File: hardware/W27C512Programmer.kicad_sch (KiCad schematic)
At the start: 124 parts, among them J1 CTRL, J2 MSB, J3 LSB, J4 Ext_UART, J5 OLED, J6 VP, J7 SAO, J8 Conn_01x02, Q1 MMBT3904, Q10 MMBT3906, Q11 MMBT3904, Q12 MMBT3906, Q2 MMBT3906, Q3 MMBT3904, Q4 MMBT3904, Q5 MMBT3904, Q6 MMBT3906, Q7 MMBT3906, Q8 MMBT3906, Q9 MMBT3904, SW1 RST, SW2 USR, U1 MIC2288, U2 74HC573, U3 74HC573, U4 74HC573, U5 28/32 pin ROM

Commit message: Rev2
Untested!
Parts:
- A1, C11, J1, J2, J3, J4, J5, J6, J7, J8, JP4, JP5, U5: now not fitted
- C10: footprint Capacitor_SMD:CP_Elec_6.3x5.4 -> Capacitor_SMD:CP_Elec_6.3x7.7; LCSC C131120 -> C22388053
- C12, C2, C3, C4, C5, C6, C7, C8: footprint Capacitor_SMD:C_0603_1608Metric -> Capacitor_SMD:C_0402_1005Metric; LCSC (none) -> C1525
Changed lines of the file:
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@@
 	(wire
 		(pts
-			(xy 270.51 48.26) (xy 282.956 48.26)
+			(xy 270.51 48.26) (xy 283.21 48.26)
 		)
 		(stroke
@@
 	(wire
 		(pts
-			(xy 274.574 82.296) (xy 282.956 82.296)
+			(xy 274.574 82.296) (xy 283.21 82.296)
 		)
 		(stroke
@@
 	(wire
 		(pts
-			(xy 282.956 82.296) (xy 282.956 48.26)
+			(xy 283.21 82.296) (xy 283.21 48.26)
 		)
 		(stroke
@@
 		(in_bom yes)
 		(on_board yes)
-		(dnp no)
+		(dnp yes)
 		(property "Reference" "J6"
 			(at 194.945 119.38 0)
@@
 		(in_bom yes)
 		(on_board yes)
-		(dnp no)
+		(dnp yes)
 		(fields_autoplaced yes)
 		(property "Reference" "J7"
@@
 			)
 		)
-		(property "Footprint" "Capacitor_SMD:C_0603_1608Metric"
+		(property "Footprint" "Capacitor_SMD:C_0402_1005Metric"
 			(at 21.59 102.87 0)
 			(effects
@@
 			)
 		)
+		(property "LCSC" "C1525"
+			(at 21.59 102.87 0)
+			(effects
+				(font
+					(size 1.27 1.27)
+				)
+				(hide yes)
+			)
+		)
 		(pin "1"
 		)
@@
 		(in_bom yes)
 		(on_board yes)
-		(dnp no)
+		(dnp yes)
 		(property "Reference" "J2"
 			(at 22.225 45.085 0)
@@
 			)
 		)
-		(property "Footprint" "Capacitor_SMD:C_0603_1608Metric"
+		(property "Footprint" "Capacitor_SMD:C_0402_1005Metric"
 			(at 69.85 102.87 0)
 			(effects
@@
 			)
 		)
+		(property "LCSC" "C1525"
+			(at 69.85 102.87 0)
+			(effects
+				(font
+					(size 1.27 1.27)
+				)
+				(hide yes)
+			)
+		)
 		(pin "1"
 		)
@@
 		(in_bom yes)
 		(on_board yes)
-		(dnp no)
+		(dnp yes)
 		(property "Reference" "J3"
 			(at 30.48 20.32 0)
@@
 		(in_bom yes)
 		(on_board yes)
-		(dnp no)
+		(dnp yes)
 		(fields_autoplaced yes)
 		(property "Reference" "J4"
@@
 			)
 		)
-		(property "Footprint" "Capacitor_SMD:C_0603_1608Metric"
+		(property "Footprint" "Capacitor_SMD:C_0402_1005Metric"
 			(at 49.53 102.87 0)
 			(effects
@@
 			)
 		)
+		(property "LCSC" "C1525"
+			(at 49.53 102.87 0)
+			(effects
+				(font
+					(size 1.27 1.27)
+				)
+				(hide yes)
+			)
+		)
 		(pin "1"
 		)
@@
 			)
 		)
-		(property "Footprint" "Capacitor_SMD:C_0603_1608Metric"
+		(property "Footprint" "Capacitor_SMD:C_0402_1005Metric"
 			(at 43.18 102.87 0)
 			(effects
@@
 			)
 		)
+		(property "LCSC" "C1525"
+			(at 43.18 102.87 0)
+			(effects
+				(font
+					(size 1.27 1.27)
+				)
+				(hide yes)
+			)
+		)
 		(pin "1"
 		)
@@
 		(in_bom yes)
 		(on_board yes)
-		(dnp no)
+		(dnp yes)
 		(fields_autoplaced yes)
 		(property "Reference" "J8"
@@
 		(in_bom yes)
 		(on_board yes)
-		(dnp no)
+		(dnp yes)
 		(fields_autoplaced yes)
 		(property "Reference" "J1"
@@
 			)
 		)
-		(property "Footprint" "Capacitor_SMD:C_0603_1608Metric"
+		(property "Footprint" "Capacitor_SMD:C_0402_1005Metric"
 			(at 27.94 102.87 0)
 			(effects
@@
 			)
 		)
+		(property "LCSC" "C1525"
+			(at 27.94 102.87 0)
+			(effects
+				(font
+					(size 1.27 1.27)
+				)
+				(hide yes)
+			)
+		)
 		(pin "1"
 		)
@@
 		(in_bom yes)
 		(on_board yes)
-		(dnp no)
+		(dnp yes)
 		(property "Reference" "JP4"
 			(at 179.07 64.77 0)
@@
 			)
 		)
-		(property "Footprint" "Capacitor_SMD:C_0603_1608Metric"
+		(property "Footprint" "Capacitor_SMD:C_0402_1005Metric"
 			(at 55.88 102.87 0)
 			(effects
@@
 			)
 		)
+		(property "LCSC" "C1525"
+			(at 55.88 102.87 0)
+			(effects
+				(font
+					(size 1.27 1.27)
+				)
+				(hide yes)
+			)
+		)
 		(pin "1"
 		)
@@
 		(in_bom yes)
 		(on_board yes)
-		(dnp no)
+		(dnp yes)
 		(fields_autoplaced yes)
 		(property "Reference" "J5"
@@
 			)
 		)
-		(property "Footprint" "Capacitor_SMD:C_0603_1608Metric"
+		(property "Footprint" "Capacitor_SMD:C_0402_1005Metric"
 			(at 62.23 102.87 0)
 			(effects
@@
 			)
 		)
+		(property "LCSC" "C1525"
+			(at 62.23 102.87 0)
+			(effects
+				(font
+					(size 1.27 1.27)
+				)
+				(hide yes)
+			)
+		)
 		(pin "1"
 		)
@@
 			)
 		)
-		(property "Footprint" "Capacitor_SMD:CP_Elec_6.3x5.4"
+		(property "Footprint" "Capacitor_SMD:CP_Elec_6.3x7.7"
 			(at 75.565 102.87 0)
 			(effects
@@
 			)
 		)
-		(property "LCSC" "C131120"
+		(property "LCSC" "C22388053"
 			(at 75.565 102.87 0)
 			(effects
@@
 		(in_bom yes)
 		(on_board yes)
-		(dnp no)
+		(dnp yes)
 		(property "Reference" "U5"
 			(at 211.5694 21.59 0)
@@
 			)
 		)
-		(property "Footprint" "Capacitor_SMD:C_0603_1608Metric"
+		(property "Footprint" "Capacitor_SMD:C_0402_1005Metric"
 			(at 34.29 102.87 0)
 			(effects
@@
 			)
 		)
+		(property "LCSC" "C1525"
+			(at 34.29 102.87 0)
+			(effects
+				(font
+					(size 1.27 1.27)
+				)
+				(hide yes)
+			)
+		)
 		(pin "1"
 		)
@@
 		(in_bom yes)
 		(on_board yes)
-		(dnp no)
+		(dnp yes)
 		(property "Reference" "C11"
 			(at 77.47 174.244 0)
@@
 		(in_bom no)
 		(on_board yes)
-		(dnp no)
+		(dnp yes)
 		(property "Reference" "JP5"
 			(at 187.706 106.934 0)
@@
 		(in_bom no)
 		(on_board yes)
-		(dnp no)
+		(dnp yes)
 		(fields_autoplaced yes)
 		(property "Reference" "A1"

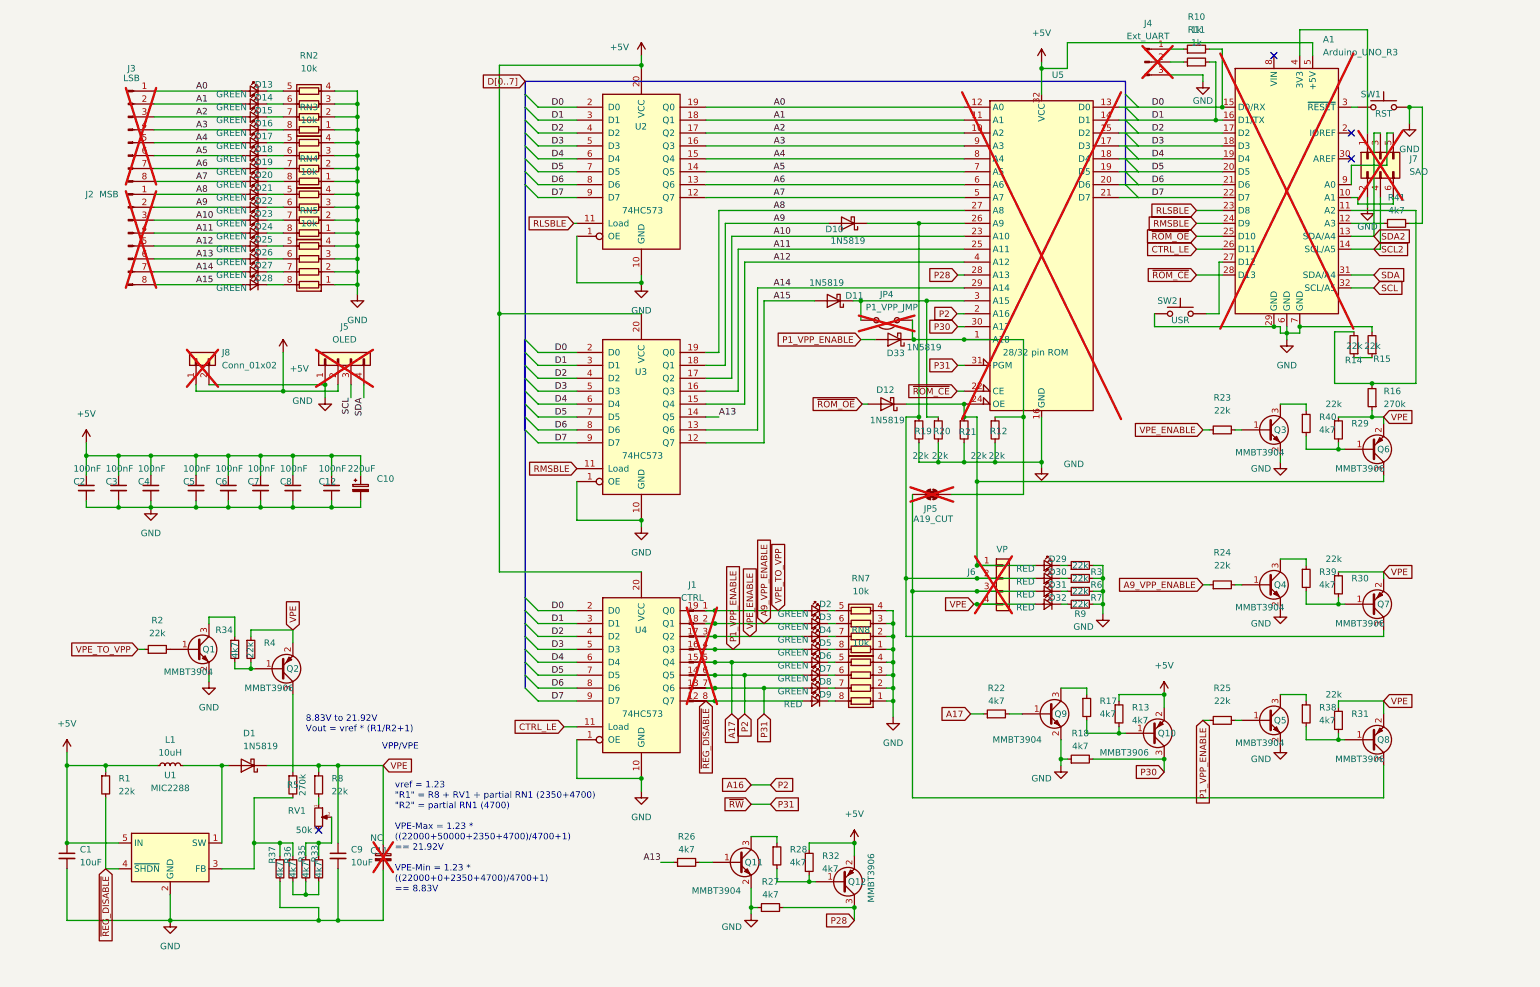
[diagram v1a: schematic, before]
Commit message: Fuse in schematic
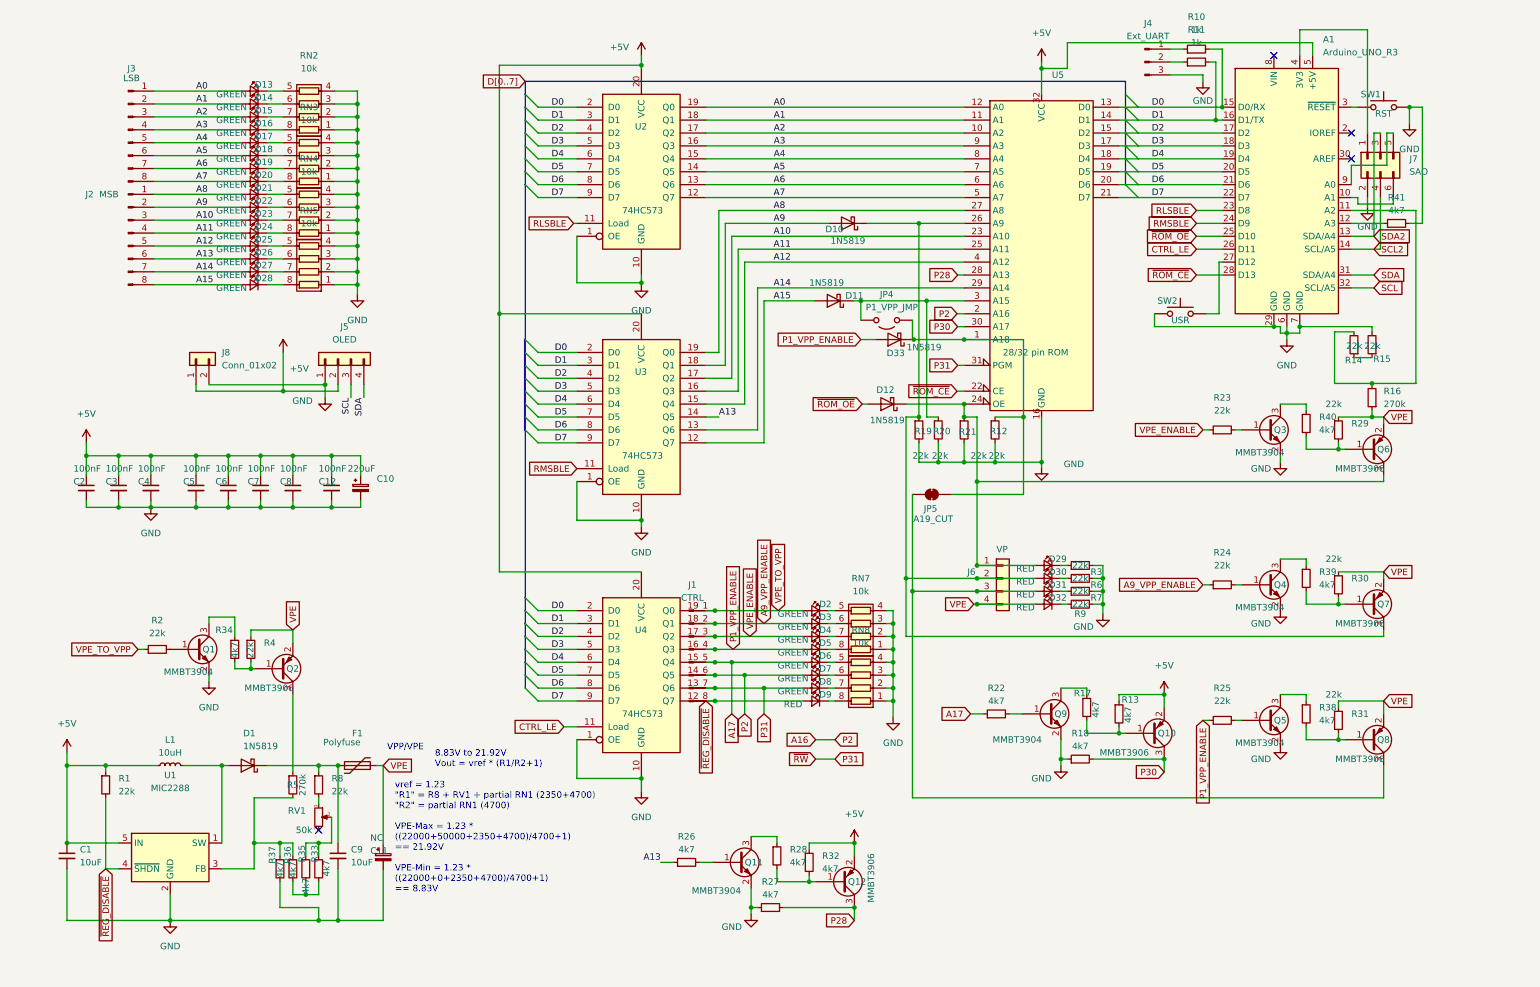
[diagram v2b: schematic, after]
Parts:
- added F1: Polyfuse, Fuse:Fuse_1812_4532Metric, symbol Device:Polyfuse
- A1, C11, J1, J2, J3, J4, J5, J6, J7, J8, JP4, JP5: now fitted
- U5: LCSC (none) -> C146583; now fitted
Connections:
- net VPE: now also F1.2; no longer C9.1, D1.1 (K), R8.1
- new net: C9.1, D1.1 (K), F1.1, R8.1
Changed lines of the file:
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@@
 	(wire
 		(pts
+			(xy 78.74 157.48) (xy 80.01 157.48)
+		)
+		(stroke
+			(width 0)
+			(type default)
+		)
+	)
+	(wire
+		(pts
 			(xy 57.15 32.385) (xy 60.325 32.385)
 		)
@@
 	(wire
 		(pts
-			(xy 71.12 157.48) (xy 80.01 157.48)
-		)
-		(stroke
-			(width 0)
-			(type default)
-		)
-	)
-	(wire
-		(pts
 			(xy 143.51 83.82) (xy 149.86 83.82)
 		)
@@
 	(wire
 		(pts
-			(xy 152.4 165.1) (xy 156.21 165.1)
+			(xy 165.1 156.21) (xy 168.91 156.21)
 		)
 		(stroke
@@
 	(wire
 		(pts
-			(xy 152.4 161.29) (xy 156.21 161.29)
+			(xy 165.1 152.4) (xy 168.91 152.4)
 		)
 		(stroke
@@
 	(text "8.83V to 21.92V \nVout = vref * (R1/R2+1)"
 		(exclude_from_sim no)
-		(at 64.77 151.13 0)
+		(at 90.17 157.988 0)
 		(effects
 			(font
@@
 	(text "VPP/VPE"
 		(exclude_from_sim no)
-		(at 79.756 154.559 0)
+		(at 80.772 154.686 0)
 		(effects
 			(font
@@
 	(global_label "P31"
 		(shape input)
-		(at 156.21 165.1 0)
+		(at 168.91 156.21 0)
 		(fields_autoplaced yes)
 		(effects
@@
 		)
 		(property "Intersheetrefs" "${INTERSHEET_REFS}"
-			(at 162.23 165.1 0)
+			(at 174.93 156.21 0)
 			(effects
 				(font
@@
 	(global_label "~{RW}"
 		(shape input)
-		(at 152.4 165.1 180)
+		(at 165.1 156.21 180)
 		(fields_autoplaced yes)
 		(effects
@@
 		)
 		(property "Intersheetrefs" "${INTERSHEET_REFS}"
-			(at 147.3476 165.1 0)
+			(at 160.0476 156.21 0)
 			(effects
 				(font
@@
 	(global_label "P2"
 		(shape input)
-		(at 156.21 161.29 0)
+		(at 168.91 152.4 0)
 		(fields_autoplaced yes)
 		(effects
@@
 		)
 		(property "Intersheetrefs" "${INTERSHEET_REFS}"
-			(at 161.0205 161.29 0)
+			(at 173.7205 152.4 0)
 			(effects
 				(font
@@
 	(global_label "A16"
 		(shape input)
-		(at 152.4 161.29 180)
+		(at 165.1 152.4 180)
 		(fields_autoplaced yes)
 		(effects
@@
 		)
 		(property "Intersheetrefs" "${INTERSHEET_REFS}"
-			(at 146.5614 161.29 0)
+			(at 159.2614 152.4 0)
 			(effects
 				(font
@@
 		(in_bom yes)
 		(on_board yes)
-		(dnp yes)
+		(dnp no)
 		(property "Reference" "J6"
 			(at 194.945 119.38 0)
@@
 		(in_bom yes)
 		(on_board yes)
-		(dnp yes)
+		(dnp no)
 		(fields_autoplaced yes)
 		(property "Reference" "J7"
@@
 		(in_bom yes)
 		(on_board yes)
-		(dnp yes)
+		(dnp no)
 		(property "Reference" "J2"
 			(at 22.225 45.085 0)
@@
 		(in_bom yes)
 		(on_board yes)
-		(dnp yes)
+		(dnp no)
 		(property "Reference" "J3"
 			(at 30.48 20.32 0)
@@
 		(in_bom yes)
 		(on_board yes)
-		(dnp yes)
+		(dnp no)
 		(fields_autoplaced yes)
 		(property "Reference" "J4"
@@
 		)
 		(property "Value" "4k7"
-			(at 67.31 179.578 90)
+			(at 68.834 179.324 90)
 			(effects
 				(font
@@
 		(in_bom yes)
 		(on_board yes)
-		(dnp yes)
+		(dnp no)
 		(fields_autoplaced yes)
 		(property "Reference" "J8"
@@
 		(in_bom yes)
 		(on_board yes)
-		(dnp yes)
+		(dnp no)
 		(fields_autoplaced yes)
 		(property "Reference" "J1"
@@
 		(on_board yes)
 		(dnp no)
-		(fields_autoplaced yes)
 		(property "Reference" "R13"
-			(at 227.33 146.0499 0)
+			(at 225.298 144.526 0)
 			(effects
 				(font
@@
 		)
 		(property "Value" "4k7"
-			(at 227.33 148.5899 0)
+			(at 226.568 149.098 90)
 			(effects
 				(font
@@
 	)
 	(symbol
+		(lib_id "Device:Polyfuse")
+		(at 74.93 157.48 90)
+		(unit 1)
+		(exclude_from_sim no)
+		(in_bom yes)
+		(on_board yes)
+		(dnp no)
+		(property "Reference" "F1"
+			(at 74.93 151.13 90)
+			(effects
+				(font
+					(size 1.27 1.27)
+				)
+			)
+		)
+		(property "Value" "Polyfuse"
+			(at 71.882 152.908 90)
+			(effects
+				(font
+					(size 1.27 1.27)
+				)
+			)
+		)
+		(property "Footprint" "Fuse:Fuse_1812_4532Metric"
+			(at 80.01 156.21 0)
+			(effects
+				(font
+					(size 1.27 1.27)
+				)
+				(justify left)
+				(hide yes)
+			)
+		)
+		(property "Datasheet" "~"
+			(at 74.93 157.48 0)
+			(effects
+				(font
+					(size 1.27 1.27)
+				)
+				(hide yes)
+			)
+		)
+		(property "Description" "Resettable fuse, polymeric positive temperature coefficient"
+			(at 74.93 157.48 0)
+			(effects
+				(font
+					(size 1.27 1.27)
+				)
+				(hide yes)
+			)
+		)
+		(property "LCSC" "C269125"
+			(at 74.93 157.48 0)
+			(effects
+				(font
+					(size 1.27 1.27)
+				)
+				(hide yes)
+			)
+		)
+		(pin "2"
+		)
+		(pin "1"
+		)
+		(instances
+			(project ""
+				(path "/019f16b9-c943-44db-aa5e-c001925deb8a"
+					(reference "F1")
+					(unit 1)
+				)
+			)
+		)
+	)
+	(symbol
 		(lib_id "power:+5V")
 		(at 172.72 172.72 0)
@@
 		(in_bom yes)
 		(on_board yes)
-		(dnp yes)
+		(dnp no)
 		(property "Reference" "JP4"
 			(at 179.07 64.77 0)
@@
 		(in_bom yes)
 		(on_board yes)
-		(dnp yes)
+		(dnp no)
 		(fields_autoplaced yes)
 		(property "Reference" "J5"
@@
 		(in_bom yes)
 		(on_board yes)
-		(dnp yes)
+		(dnp no)
 		(property "Reference" "U5"
 			(at 211.5694 21.59 0)
@@
 			)
 		)
+		(property "LCSC" "C146583"
+			(at 209.55 58.42 0)
+			(effects
+				(font
+					(size 1.27 1.27)
+				)
+				(hide yes)
+			)
+		)
 		(pin "16"
 		)
@@
 		(in_bom yes)
 		(on_board yes)
-		(dnp yes)
+		(dnp no)
 		(property "Reference" "C11"
 			(at 77.47 174.244 0)
@@
 					(size 1.27 1.27)
 				)
-				(justify left)
+				(justify right)
 			)
 		)
@@
 		(in_bom no)
 		(on_board yes)
-		(dnp yes)
+		(dnp no)
 		(property "Reference" "JP5"
 			(at 187.706 106.934 0)
@@
 		(in_bom no)
 		(on_board yes)
-		(dnp yes)
+		(dnp no)
 		(fields_autoplaced yes)
 		(property "Reference" "A1"
@@
 		(on_board yes)
 		(dnp no)
-		(fields_autoplaced yes)
 		(property "Reference" "R17"
-			(at 220.98 144.7799 0)
+			(at 215.9 143.256 0)
 			(effects
 				(font
@@
 		)
 		(property "Value" "4k7"
-			(at 220.98 147.3199 0)
+			(at 220.218 148.082 90)
 			(effects
 				(font

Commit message: Rev2.1
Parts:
- removed R33: 4k7, Resistor_SMD:R_0402_1005Metric, symbol Device:R_Small
- added JP6, JP8, JP9: Bodge point, Jumper:SolderJumper-2_P1.3mm_Bridged_RoundedPad1.0x1.5mm, symbol Jumper:SolderJumper_2_Bridged
- added JP7: Tin foil socket, Jumper:SolderJumper-2_P1.3mm_Open_RoundedPad1.0x1.5mm, symbol Jumper:SolderJumper_2_Open
- added R42: 4k7, Resistor_SMD:R_0402_1005Metric, symbol Device:R_Small
- added TP1: TestPoint, TestPoint:TestPoint_Pad_D3.0mm, symbol Connector:TestPoint
- F1: footprint Fuse:Fuse_1812_4532Metric -> Fuse:Fuse_0805_2012Metric; LCSC C269125 -> C516070
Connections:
- net +5V: now also F1.1, JP7.2 (B); no longer C1.1, C8.1, L1.1, R1.1, U1.5 (IN)
- net GND: now also R42.2, TP1.1
- net VPE: now also C9.1, D1.1 (K), JP8.2 (B); no longer F1.2
- net FB: now reaches R5.2, U1.3 (FB)
- net FB: now also JP6.1 (A), JP9.2 (B); no longer R36.1, R37.1
- net at R35.1, RV1.2: now also RV1.3
- net at A1.12 (A3), R41.1: now also R42.1
- new net 5V_REG: C1.1, C8.1, F1.2, JP7.1 (A), L1.1, R1.1, U1.5 (IN)
- new net R1E: JP6.2 (B), R36.1
- new net R1S: JP8.1 (A), R8.1
- new net Rf2: JP9.1 (A), R37.1
- no-connect marks 4 -> 3
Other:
- note added: ""R1" at 14V VPE = 48.8k 48.8k in parallel with 270k = 41.33k 1.23*(41.33k/4700+1) = 12.05V VPP"
- note added: "Revision Resistors 4k7 = Rev2 2350 = Rev2.1"
- note added: "vref = 1.23 "R1" = R8 + RV1 + R35 + R36 "R2" = R37 (4700) VPE-Max = 1.23 * ((22000+50000+4700+4700)/4700+1) == 22.53V VPE-Min = 1.23 * ((22000+0+4700+4700)/4700+1) == 9.45V"
- note removed: "vref = 1.23 "R1" = R8 + RV1 + partial RN1 (2350+4700) "R2" = partial RN1 (4700) VPE-Max = 1.23 * ((22000+50000+2350+4700)/4700+1) == 21.92V VPE-Min = 1.23 * ((22000+0+2350+4700)/4700+1) == 8.83V"
- moved on the sheet: C8, C9, D1, D13, D14, D15, D16, D17, D18, D19, D20, D21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
